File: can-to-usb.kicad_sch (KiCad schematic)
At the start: 23 parts, among them Q10 AO3400A, Q5 AO3400A, Q8 AO3401A, U13 STM32G431CBU6, U15 TJA1044GTK_3Z

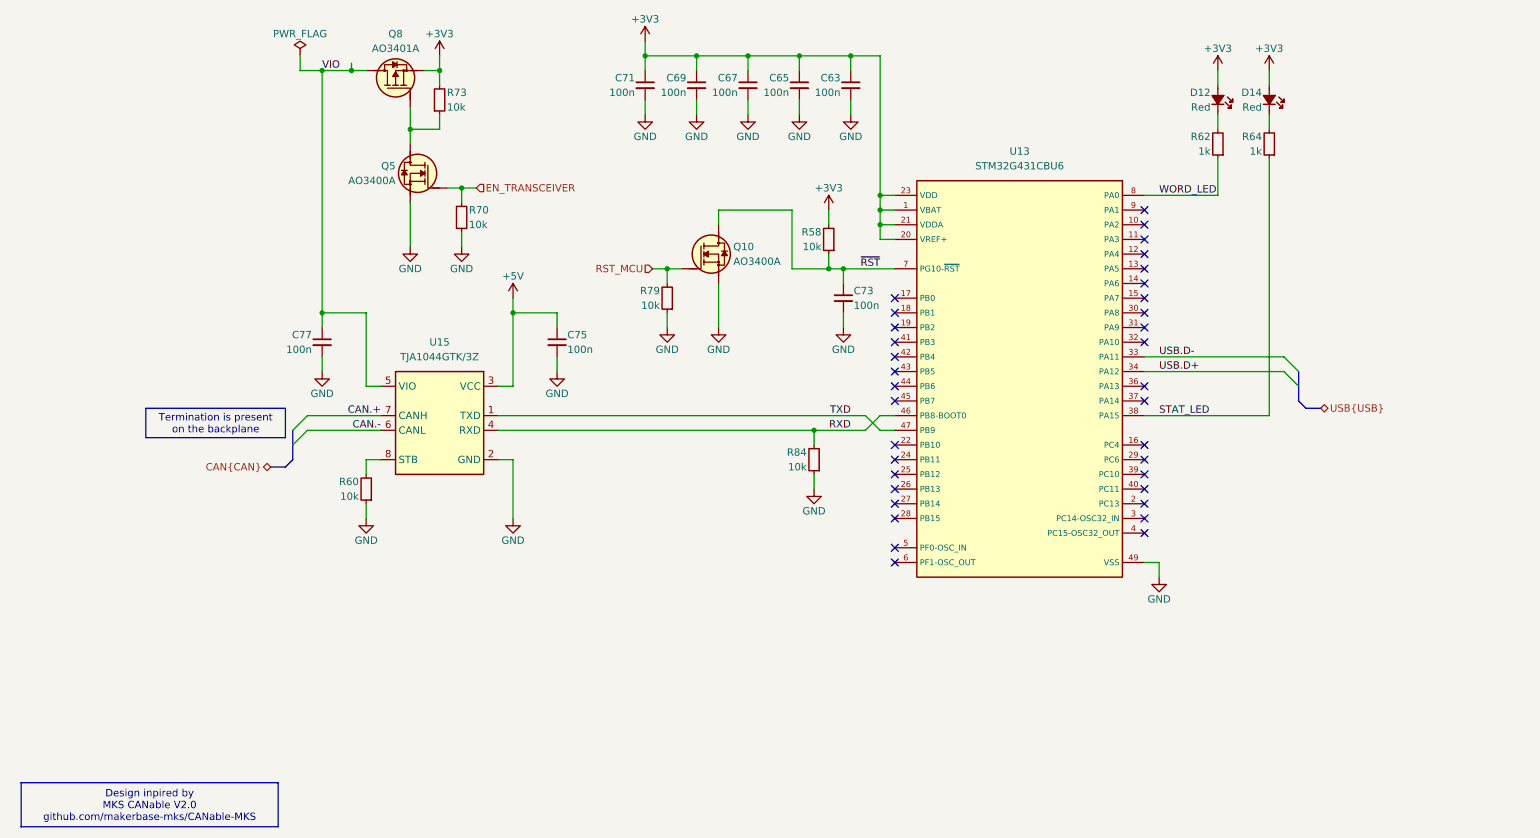
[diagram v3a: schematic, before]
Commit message: [#3] Continue layout, minor schematic fixes, add power switch for CAN transceiver 5V rail
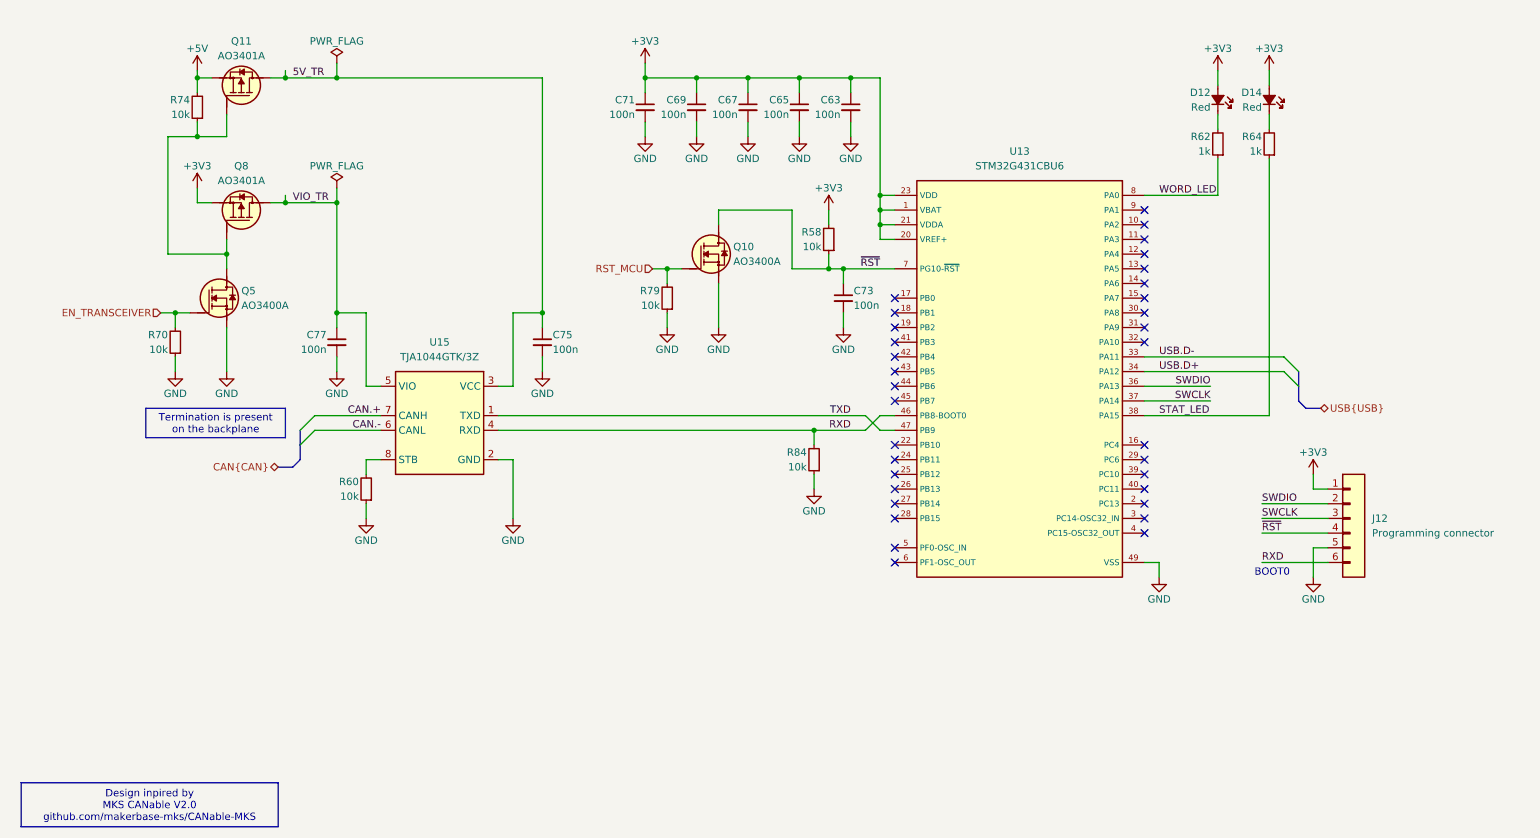
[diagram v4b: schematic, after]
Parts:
- added J12: Programming connector, DW-footprints:Custom-programming-connector-1x6_P1.27mm, symbol DW-connectors:Custom-programming-connector-1x6_P1.27mm
- added Q11: AO3401A, DW-footprints:SOT-23-3, symbol DW-transistors:AO3401A
- renumbered R73 to R74
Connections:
- net +3V3: now also J12.1; no longer R74.2
- net +5V: now also R74.2, Q11.2 (S); no longer C75.1, U15.3 (VCC)
- net GND: now also J12.5
- net RXD: now also J12.6
- net ~{RST}: now also J12.4
- net SWDIO: now reaches U13.36 (PA13)
- net SWDIO: now also J12.2
- net SWCLK: now reaches U13.37 (PA14)
- net SWCLK: now also J12.3
- net at Q5.3 (D), Q8.1 (G), R74.1: now also Q11.1 (G)
- net VIO renamed VIO_TR
- new net 5V_TR: C75.1, Q11.3 (D), U15.3 (VCC)
- no-connect marks 35 -> 33
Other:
- note added: "BOOT0"
- moved on the sheet: C63, C65, C67, C69, C71, C75, C77, Q5, Q8, R70, R74

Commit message: [#3] WIP: Clear ERC, re-annotate schematic
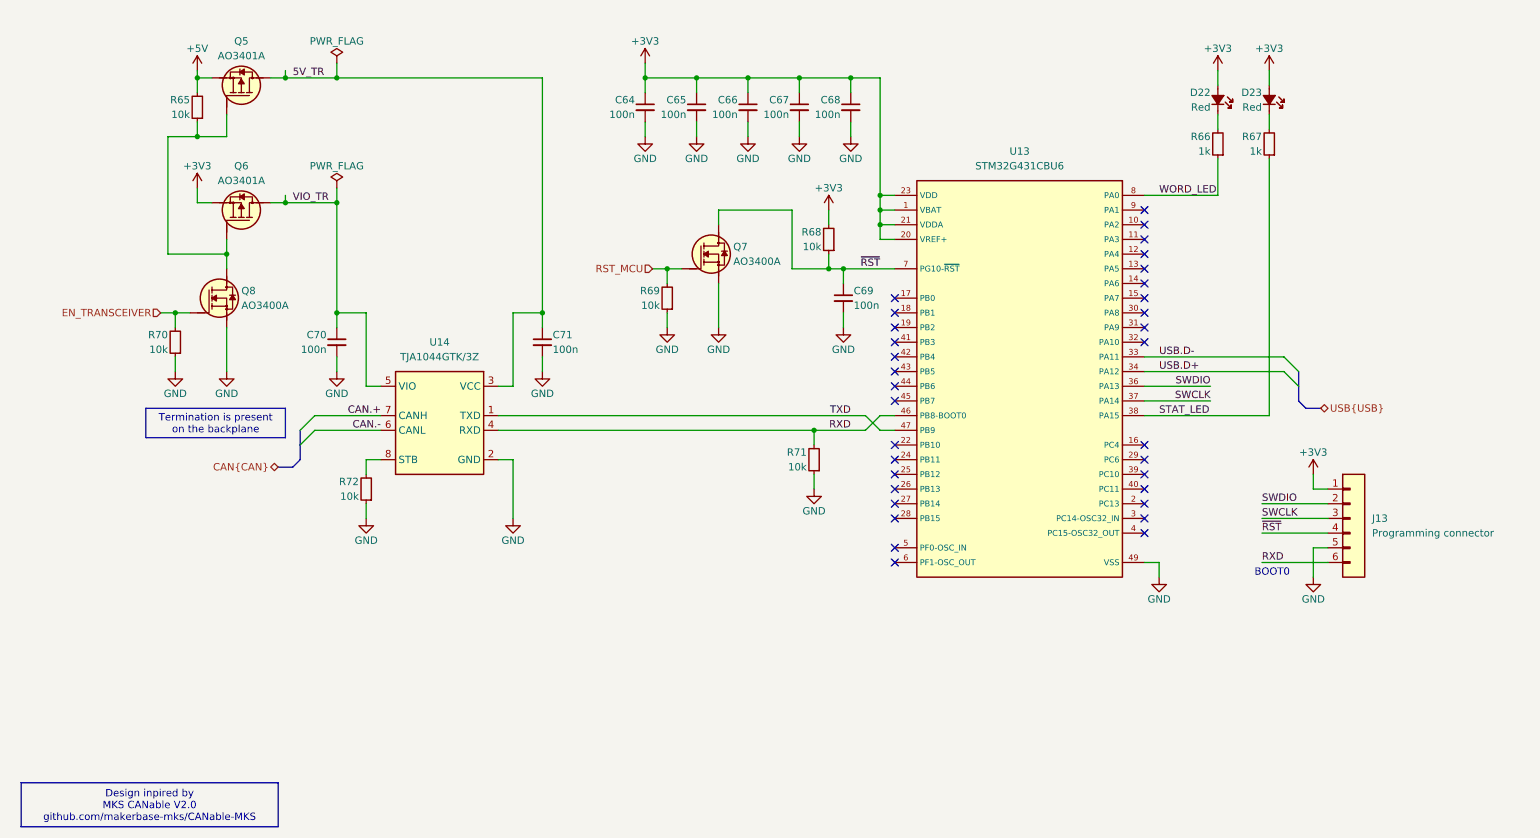
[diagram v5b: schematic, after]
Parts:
- renumbered C71 to C64, C69 to C65, C67 to C66, C65 to C67, C63 to C68, C73 to C69, C77 to C70, C75 to C71, D12 to D22, D14 to D23, J12 to J13, Q11 to Q5, Q8 to Q6, Q10 to Q7, Q5 to Q8, R74 to R65, R62 to R66, R64 to R67, R58 to R68, R79 to R69, R84 to R71, R60 to R72, U15 to U14

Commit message: [#3] Re-annotate schematic
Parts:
- renumbered C64 to C60, C65 to C61, C66 to C62, C67 to C63, C68 to C64, C69 to C65, C70 to C66, C71 to C67, D22 to D18, D23 to D19, J13 to J11, R65 to R67, R66 to R68, R67 to R69, R68 to R70, R69 to R71, R70 to R72, R71 to R73, R72 to R74
